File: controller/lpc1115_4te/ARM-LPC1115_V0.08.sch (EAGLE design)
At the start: 53 parts, among them IC1 LPC1115, IC2 MC34063AP, IC3 MCP1702-33, Q1 BC557B, Q3 BC640C, Q4 12MHz, T1 BC547C

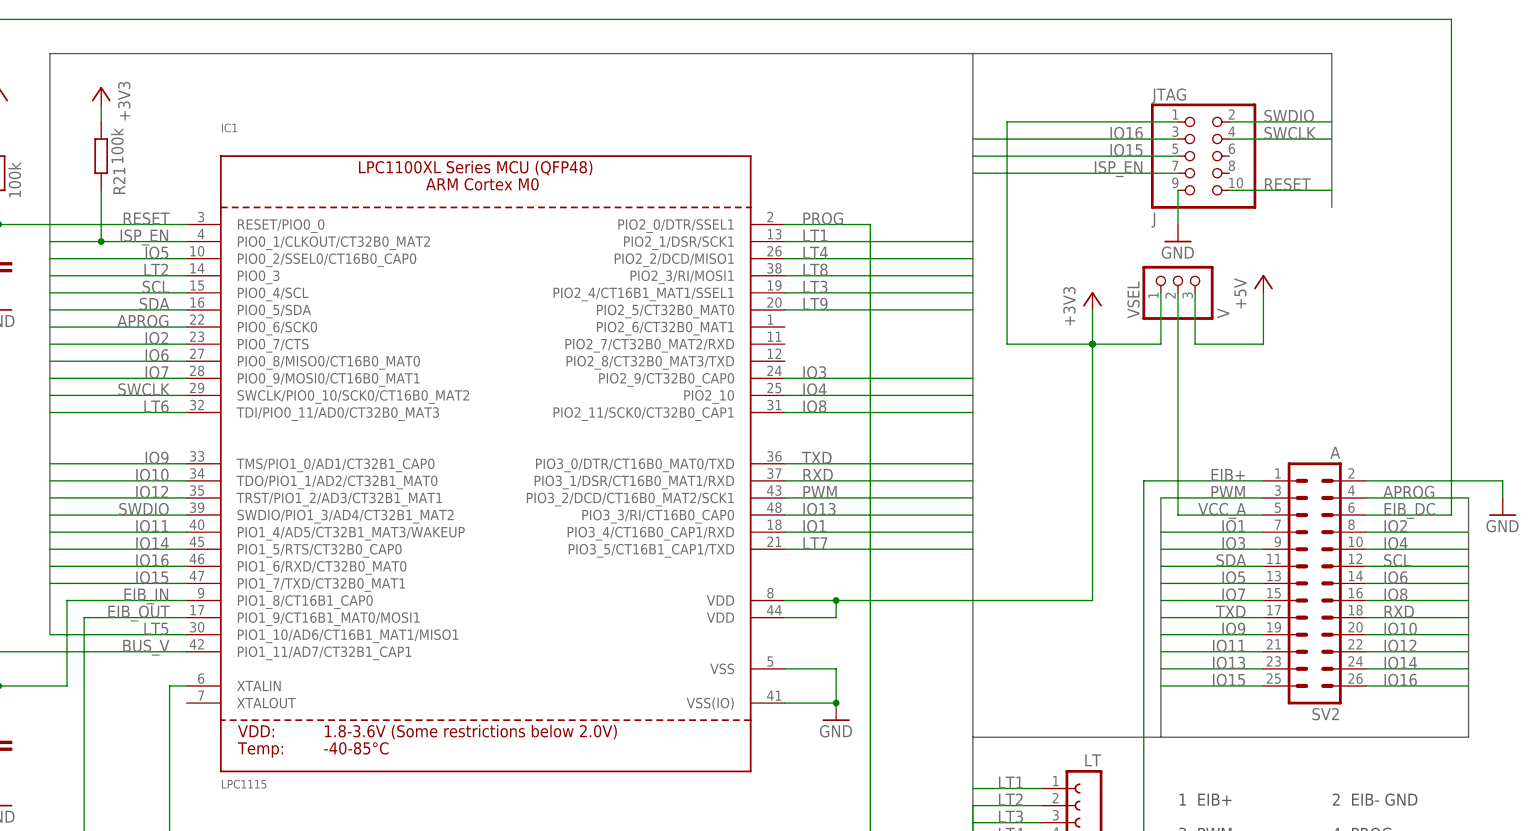
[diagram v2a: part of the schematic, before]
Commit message: Additional GND added to App pinheader
On pin 21 a new GND has been added. The following pins have been rearraged
to keep all ADV channels.
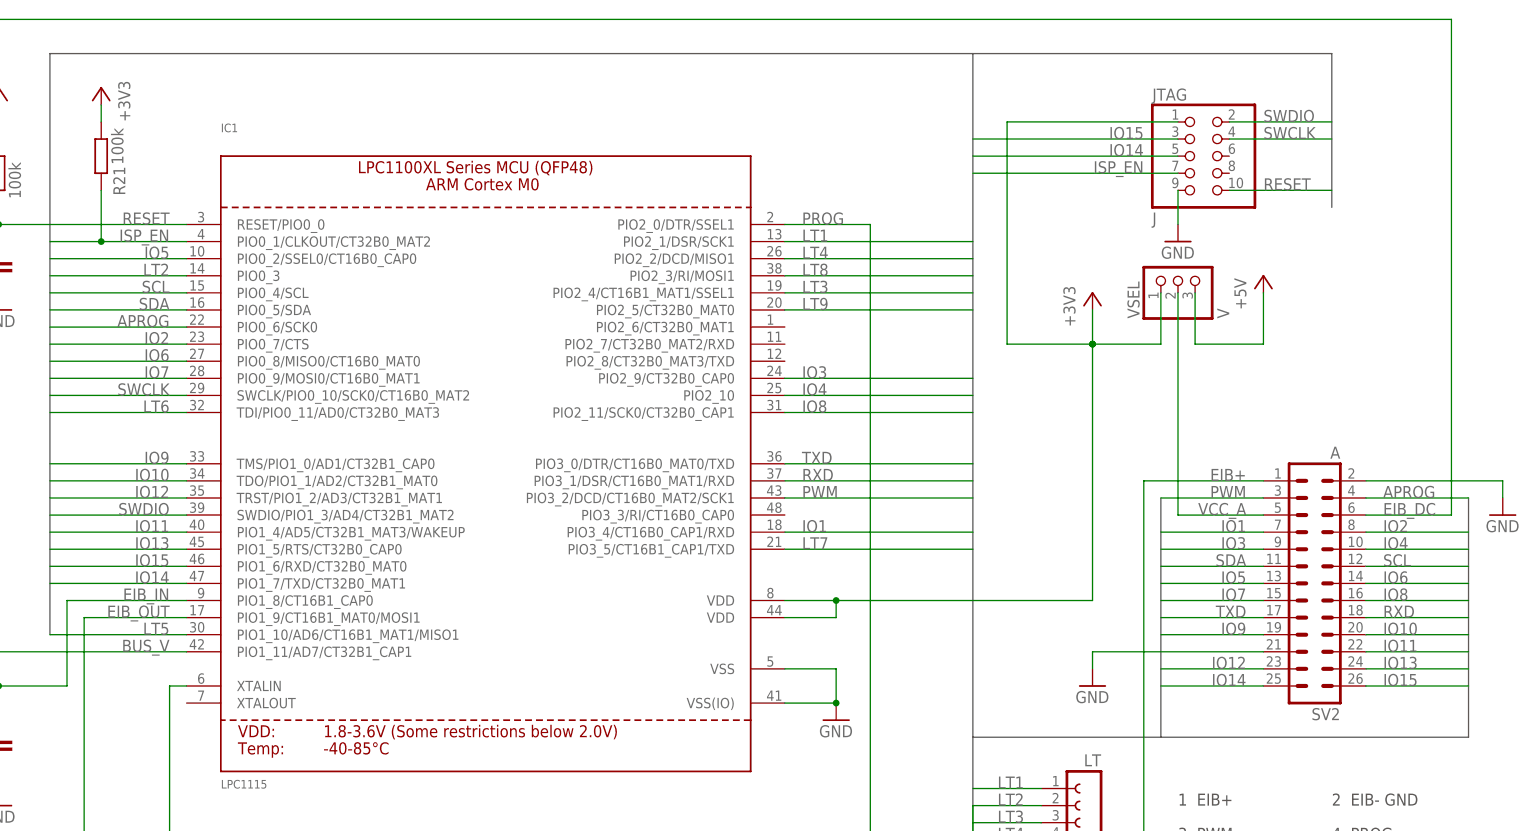
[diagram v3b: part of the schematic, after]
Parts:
- JTAG: device microbuilder:HEADER-2X5 -> pinhead-2:PINHD-2X05_2.00
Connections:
- removed net IO16: IC1.PIO1_6/RXD/CT32B0_MAT0, JTAG.3, SV2.26
- net GND: now also SV2.21
- net IO11: now also SV2.22; no longer SV2.21
- net IO12: now also SV2.23; no longer SV2.22
- net IO13: now also IC1.PIO1_5/RTS/CT32B0_CAP0, SV2.24; no longer IC1.PIO3_3/RI/CT16B0_CAP0, SV2.23
- net IO14: now also IC1.PIO1_7/TXD/CT32B0_MAT1, JTAG.5, SV2.25; no longer IC1.PIO1_5/RTS/CT32B0_CAP0, SV2.24
- net IO15: now also IC1.PIO1_6/RXD/CT32B0_MAT0, JTAG.3, SV2.26; no longer IC1.PIO1_7/TXD/CT32B0_MAT1, JTAG.5, SV2.25
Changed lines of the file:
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@@
 <part name="SV1" library="con-lsta" deviceset="FE12-1" device="" value="LT"/>
 <part name="SV2" library="con-harting-ml" deviceset="ML26" device="" value="A"/>
-<part name="JTAG" library="microbuilder" deviceset="HEADER-2X5" device="" value="J"/>
+<part name="JTAG" library="pinhead-2" deviceset="PINHD-2X05" device="_2.00" value="J"/>
 <part name="GND24" library="supply1" deviceset="GND" device=""/>
 <part name="R4" library="rcl" deviceset="R-EU_" device="0204/7" value="100k"/>
@@
 <part name="P+1" library="supply1" deviceset="+5V" device=""/>
 <part name="C11" library="rcl" deviceset="C-EU" device="050-024X044" value="100n"/>
+<part name="GND6" library="supply1" deviceset="GND" device=""/>
 </parts>
 <sheets>
@@
 <instance part="P+1" gate="1" x="0" y="157.48"/>
 <instance part="C11" gate="G$1" x="63.5" y="73.66" rot="R90"/>
+<instance part="GND6" gate="1" x="254" y="53.34"/>
 </instances>
 <busses>
-<bus name="IO[1..16],LT[1..9],SCL,SDA,PWM,APROG,RXD,TXD,RESET,SWCLK,SWDIO,ISP_EN">
+<bus name="IO[1..15],LT[1..9],SCL,SDA,PWM,APROG,RXD,TXD,RESET,SWCLK,SWDIO,ISP_EN">
 <segment>
 <wire x1="236.22" y1="45.72" x2="264.16" y2="45.72" width="0.762" layer="92"/>
@@
 <pinref part="GND17" gate="1" pin="GND"/>
 <wire x1="20.32" y1="127" x2="20.32" y2="129.54" width="0.1524" layer="91"/>
+</segment>
+<segment>
+<pinref part="SV2" gate="1" pin="21"/>
+<wire x1="279.4" y1="58.42" x2="254" y2="58.42" width="0.1524" layer="91"/>
+<pinref part="GND6" gate="1" pin="GND"/>
+<wire x1="254" y1="58.42" x2="254" y2="55.88" width="0.1524" layer="91"/>
 </segment>
 </net>
@@
 </segment>
 <segment>
-<pinref part="SV2" gate="1" pin="22"/>
-<wire x1="294.64" y1="58.42" x2="309.88" y2="58.42" width="0.1524" layer="91"/>
-<label x="297.18" y="58.42" size="1.778" layer="95"/>
-</segment>
-</net>
-<net name="IO13" class="0">
-<segment>
-<pinref part="IC1" gate="G$1" pin="PIO3_3/RI/CT16B0_CAP0"/>
-<wire x1="236.22" y1="78.74" x2="208.28" y2="78.74" width="0.1524" layer="91"/>
-<label x="210.82" y="78.74" size="1.778" layer="95"/>
-</segment>
-<segment>
 <pinref part="SV2" gate="1" pin="23"/>
 <wire x1="279.4" y1="55.88" x2="264.16" y2="55.88" width="0.1524" layer="91"/>
@@
 </segment>
 </net>
-<net name="IO15" class="0">
-<segment>
-<pinref part="IC1" gate="G$1" pin="PIO1_7/TXD/CT32B0_MAT1"/>
-<wire x1="99.06" y1="68.58" x2="119.38" y2="68.58" width="0.1524" layer="91"/>
-<label x="116.84" y="68.58" size="1.778" layer="95" rot="MR0"/>
-</segment>
-<segment>
-<pinref part="JTAG" gate="A" pin="5"/>
-<wire x1="236.22" y1="132.08" x2="266.7" y2="132.08" width="0.1524" layer="91"/>
-<label x="261.62" y="132.08" size="1.778" layer="95" rot="MR0"/>
-</segment>
-<segment>
-<pinref part="SV2" gate="1" pin="25"/>
-<wire x1="279.4" y1="53.34" x2="264.16" y2="53.34" width="0.1524" layer="91"/>
-<label x="276.86" y="53.34" size="1.778" layer="95" rot="MR0"/>
-</segment>
-</net>
 <net name="LT9" class="0">
 <segment>
@@
 <wire x1="99.06" y1="111.76" x2="119.38" y2="111.76" width="0.1524" layer="91"/>
 <label x="116.84" y="111.76" size="1.778" layer="95" rot="MR0"/>
-</segment>
-</net>
-<net name="IO16" class="0">
-<segment>
-<pinref part="IC1" gate="G$1" pin="PIO1_6/RXD/CT32B0_MAT0"/>
-<wire x1="99.06" y1="71.12" x2="119.38" y2="71.12" width="0.1524" layer="91"/>
-<label x="116.84" y="71.12" size="1.778" layer="95" rot="MR0"/>
-</segment>
-<segment>
-<pinref part="JTAG" gate="A" pin="3"/>
-<wire x1="236.22" y1="134.62" x2="266.7" y2="134.62" width="0.1524" layer="91"/>
-<label x="261.62" y="134.62" size="1.778" layer="95" rot="MR0"/>
-</segment>
-<segment>
-<pinref part="SV2" gate="1" pin="26"/>
-<wire x1="294.64" y1="53.34" x2="309.88" y2="53.34" width="0.1524" layer="91"/>
-<label x="297.18" y="53.34" size="1.778" layer="95"/>
 </segment>
 </net>
@@
 </segment>
 </net>
-<net name="IO14" class="0">
-<segment>
-<pinref part="IC1" gate="G$1" pin="PIO1_5/RTS/CT32B0_CAP0"/>
-<wire x1="99.06" y1="73.66" x2="119.38" y2="73.66" width="0.1524" layer="91"/>
-<label x="116.84" y="73.66" size="1.778" layer="95" rot="MR0"/>
-</segment>
-<segment>
-<pinref part="SV2" gate="1" pin="24"/>
-<wire x1="294.64" y1="55.88" x2="309.88" y2="55.88" width="0.1524" layer="91"/>
-<label x="297.18" y="55.88" size="1.778" layer="95"/>
-</segment>
-</net>
 <net name="LT4" class="0">
 <segment>
@@
 <net name="IO11" class="0">
 <segment>
-<pinref part="SV2" gate="1" pin="21"/>
-<wire x1="279.4" y1="58.42" x2="264.16" y2="58.42" width="0.1524" layer="91"/>
-<label x="276.86" y="58.42" size="1.778" layer="95" rot="MR0"/>
-</segment>
-<segment>
 <pinref part="IC1" gate="G$1" pin="PIO1_4/AD5/CT32B1_MAT3/WAKEUP"/>
 <wire x1="99.06" y1="76.2" x2="119.38" y2="76.2" width="0.1524" layer="91"/>
 <label x="116.84" y="76.2" size="1.778" layer="95" rot="MR0"/>
 </segment>
-</net>
+<segment>
+<pinref part="SV2" gate="1" pin="22"/>
+<wire x1="294.64" y1="58.42" x2="309.88" y2="58.42" width="0.1524" layer="91"/>
+<label x="297.18" y="58.42" size="1.778" layer="95"/>
+</segment>
+</net>
+<net name="IO13" class="0">
+<segment>
+<pinref part="SV2" gate="1" pin="24"/>
+<wire x1="294.64" y1="55.88" x2="309.88" y2="55.88" width="0.1524" layer="91"/>
+<label x="297.18" y="55.88" size="1.778" layer="95"/>
+</segment>
+<segment>
+<pinref part="IC1" gate="G$1" pin="PIO1_5/RTS/CT32B0_CAP0"/>
+<wire x1="99.06" y1="73.66" x2="119.38" y2="73.66" width="0.1524" layer="91"/>
+<label x="116.84" y="73.66" size="1.778" layer="95" rot="MR0"/>
+</segment>
+</net>
+<net name="IO14" class="0">
+<segment>
+<pinref part="IC1" gate="G$1" pin="PIO1_7/TXD/CT32B0_MAT1"/>
+<wire x1="99.06" y1="68.58" x2="119.38" y2="68.58" width="0.1524" layer="91"/>
+<label x="116.84" y="68.58" size="1.778" layer="95" rot="MR0"/>
+</segment>
+<segment>
+<pinref part="JTAG" gate="A" pin="5"/>
+<wire x1="236.22" y1="132.08" x2="266.7" y2="132.08" width="0.1524" layer="91"/>
+<label x="261.62" y="132.08" size="1.778" layer="95" rot="MR0"/>
+</segment>
+<segment>
+<pinref part="SV2" gate="1" pin="25"/>
+<wire x1="279.4" y1="53.34" x2="264.16" y2="53.34" width="0.1524" layer="91"/>
+<label x="276.86" y="53.34" size="1.778" layer="95" rot="MR0"/>
+</segment>
+</net>
+<net name="IO15" class="0">
+<segment>
+<pinref part="SV2" gate="1" pin="26"/>
+<wire x1="294.64" y1="53.34" x2="309.88" y2="53.34" width="0.1524" layer="91"/>
+<label x="297.18" y="53.34" size="1.778" layer="95"/>
+</segment>
+<segment>
+<pinref part="JTAG" gate="A" pin="3"/>
+<wire x1="236.22" y1="134.62" x2="266.7" y2="134.62" width="0.1524" layer="91"/>
+<label x="261.62" y="134.62" size="1.778" layer="95" rot="MR0"/>
+</segment>
+<segment>
+<pinref part="IC1" gate="G$1" pin="PIO1_6/RXD/CT32B0_MAT0"/>
+<wire x1="99.06" y1="71.12" x2="119.38" y2="71.12" width="0.1524" layer="91"/>
+<label x="116.84" y="71.12" size="1.778" layer="95" rot="MR0"/>
+</segment>
+</net>
